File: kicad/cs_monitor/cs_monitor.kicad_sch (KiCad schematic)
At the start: 130 parts, among them J1 Conn_01x01_Female, J2 Conn_01x01_Female, J3 Conn_01x01_Female, J4 Conn, J5 Conn_01x01_Female, J6 Conn_01x01_Female, J7 Conn_01x01_Female, J8 Conn_01x01_Female, J9 Conn_01x01_Female, Q1 5N10, Q2 Q_NMOS_GSD, T1 HY931147C, U1 W5500, U2 OPA354AIDBVR, U3 LM2733XMF, U4 LMR50410XDBVR, U5 NCP1117-3.3, U6 MCP1700x, Y1 25MHz, Y2 16

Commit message: удалено:       kicad/cs_monitor/#auto_saved_files# 	удалено:       kicad/cs_monitor/_autosave-cs_monitor.kicad_pcb 	удалено:       kicad/cs_monitor/_autosave-cs_monitor.kicad_sch 	удалено:       kicad/cs_monitor/cs_monitor-backups/cs_monitor-2025-07-08_182651.zip 	удалено:       kicad/cs_monitor/cs_monitor-backups/cs_monitor-2025-07-08_184111.zip 	удалено:       kicad/cs_monitor/cs_monitor-backups/cs_monitor-2025-07-18_140158.zip 	удалено:       kicad/cs_monitor/cs_monitor-backups/cs_monitor-2025-07-18_141545.zip 	изменено:      kicad/cs_monitor/cs_monitor.kicad_pcb 	изменено:      kicad/cs_monitor/cs_monitor.kicad_prl 	изменено:      kicad/cs_monitor/cs_monitor.kicad_sch 	удалено:       kicad/cs_monitor/~_autosave-cs_monitor.kicad_pcb.lck 	удалено:       kicad/cs_monitor/~cs_monitor.kicad_sch.lck 	изменено:      stm32cubeide/SC_Monitor/Core/Inc/networkint.h 	изменено:      stm32cubeide/SC_Monitor/Core/Src/network_int.c 	изменено:      stm32cubeide/SC_Monitor/Release/Core/Src/AD5245.d 	изменено:      stm32cubeide/SC_Monitor/Release/Core/Src/main.d 	изменено:      stm32cubeide/SC_Monitor/Release/Core/Src/network_int.cyclo 	изменено:      stm32cubeide/SC_Monitor/Release/Core/Src/network_int.d 	изменено:      stm32cubeide/SC_Monitor/Release/Core/Src/network_int.o 	изменено:      stm32cubeide/SC_Monitor/Release/Core/Src/network_int.su 	изменено:      stm32cubeide/SC_Monitor/Release/Core/Src/ssd1306.d 	изменено:      stm32cubeide/SC_Monitor/Release/Core/Src/stm32g4xx_hal_msp.d 	изменено:      stm32cubeide/SC_Monitor/Release/Core/Src/stm32g4xx_it.d 	изменено:      stm32cubeide/SC_Monitor/Release/Core/Src/subdir.mk 	изменено:      stm32cubeide/SC_Monitor/Release/SC_Monitor.elf 	изменено:      stm32cubeide/SC_Monitor/Release/SC_Monitor.list 	изменено:      stm32cubeide/SC_Monitor/Release/SC_Monitor.map 	изменено:      stm32cubeide/SC_Monitor/Release/objects.list 	изменено:      stm32cubeide/WEB_Interface/test_line.html  	stm32cubeide/SC_Monitor/Core/Inc/webpages.h  	stm32cu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
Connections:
- net INT_ETH: now also D2.25 (pb11); no longer D2.26 (pb12)
- net SS_ETH: now also D2.26 (pb12); no longer D2.25 (pb11)
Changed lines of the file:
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@@
 	(global_label "INT_ETH"
 		(shape input)
-		(at 100.33 77.47 0)
+		(at 100.33 74.93 0)
 		(fields_autoplaced yes)
 		(effects
@@
 		)
 		(property "Intersheetrefs" "${INTERSHEET_REFS}"
-			(at 110.6328 77.47 0)
+			(at 110.6328 74.93 0)
 			(effects
 				(font
@@
 	(global_label "SS_ETH"
 		(shape input)
-		(at 100.33 74.93 0)
+		(at 100.33 77.47 0)
 		(fields_autoplaced yes)
 		(effects
@@
 		)
 		(property "Intersheetrefs" "${INTERSHEET_REFS}"
-			(at 110.1489 74.93 0)
+			(at 110.1489 77.47 0)
 			(effects
 				(font

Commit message: удалено:       kicad/cs_monitor/cs_monitor-backups/cs_monitor-2025-07-08_184829.zip 	удалено:       kicad/cs_monitor/cs_monitor-backups/cs_monitor-2025-07-08_185838.zip 	изменено:      kicad/cs_monitor/cs_monitor.kicad_pcb 	изменено:      kicad/cs_monitor/cs_monitor.kicad_pro 	изменено:      kicad/cs_monitor/cs_monitor.kicad_sch 	изменено:      kicad/cs_monitor/gerber/cs_monitor.drl 	удалено:       kicad/cs_monitor/gerber/cs_monitor_T01_0.30mm.gcode 	удалено:       kicad/cs_monitor/gerber/cs_monitor_T02_0.40mm.gcode 	удалено:       kicad/cs_monitor/gerber/cs_monitor_T03_0.70mm.gcode 	удалено:       kicad/cs_monitor/gerber/cs_monitor_T04_0.76mm.gcode 	удалено:       kicad/cs_monitor/gerber/cs_monitor_T05_1.00mm.gcode 	удалено:       kicad/cs_monitor/gerber/cs_monitor_T06_1.63mm.gcode 	изменено:      stm32cubeide/SC_Monitor/.mxproject 	изменено:      stm32cubeide/SC_Monitor/.settings/language.settings.xml 	изменено:      stm32cubeide/SC_Monitor/Core/Inc/main.h 	изменено:      stm32cubeide/SC_Monitor/Core/Src/main.c 	изменено:      stm32cubeide/SC_Monitor/Release/Core/Src/main.cyclo 	изменено:      stm32cubeide/SC_Monitor/Release/Core/Src/main.o 	изменено:      stm32cubeide/SC_Monitor/Release/Core/Src/main.su 	изменено:      stm32cubeide/SC_Monitor/Release/SC_Monitor.elf 	изменено:      stm32cubeide/SC_Monitor/Release/SC_Monitor.list 	изменено:      stm32cubeide/SC_Monitor/Release/SC_Monitor.map 	изменено:      stm32cubeide/SC_Monitor/SC_Monitor Release.launch 	изменено:      stm32cubeide/SC_Monitor/SC_Monitor.ioc
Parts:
- added C52: 10u, Capacitor_SMD:C_0402_1005Metric, symbol Device:C
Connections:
- net +3V3: now also C52.2
- net GND: now also C52.1
- net INT_ETH: now also D2.26 (pb12); no longer D2.25 (pb11)
- net SS_ETH: now also D2.25 (pb11); no longer D2.26 (pb12)
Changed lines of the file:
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@@
 	)
 	(junction
+		(at 101.6 22.86)
+		(diameter 0)
+		(color 0 0 0 0)
+	)
+	(junction
 		(at 80.01 114.3)
 		(diameter 0)
@@
 	(wire
 		(pts
+			(xy 101.6 22.86) (xy 106.68 22.86)
+		)
+		(stroke
+			(width 0)
+			(type default)
+		)
+	)
+	(wire
+		(pts
 			(xy 74.93 114.3) (xy 80.01 114.3)
 		)
@@
 	(wire
 		(pts
+			(xy 101.6 30.48) (xy 106.68 30.48)
+		)
+		(stroke
+			(width 0)
+			(type default)
+		)
+	)
+	(wire
+		(pts
 			(xy 41.91 137.16) (xy 43.18 137.16)
 		)
@@
 	(global_label "INT_ETH"
 		(shape input)
-		(at 100.33 74.93 0)
+		(at 100.33 77.47 0)
 		(fields_autoplaced yes)
 		(effects
@@
 		)
 		(property "Intersheetrefs" "${INTERSHEET_REFS}"
-			(at 110.6328 74.93 0)
+			(at 110.6328 77.47 0)
 			(effects
 				(font
@@
 	(global_label "SS_ETH"
 		(shape input)
-		(at 100.33 77.47 0)
+		(at 100.33 74.93 0)
 		(fields_autoplaced yes)
 		(effects
@@
 		)
 		(property "Intersheetrefs" "${INTERSHEET_REFS}"
-			(at 110.1489 77.47 0)
+			(at 110.1489 74.93 0)
 			(effects
 				(font
@@
 					(unit 1)
 				)
+			)
+		)
+	)
+	(symbol
+		(lib_id "Device:C")
+		(at 106.68 26.67 180)
+		(unit 1)
+		(exclude_from_sim no)
+		(in_bom yes)
+		(on_board yes)
+		(dnp no)
+		(property "Reference" "C52"
+			(at 106.68 19.685 0)
+			(effects
+				(font
+					(size 1.27 1.27)
+				)
+			)
+		)
+		(property "Value" "10u"
+			(at 106.68 21.59 0)
+			(effects
+				(font
+					(size 1.27 1.27)
+				)
+			)
+		)
+		(property "Footprint" "Capacitor_SMD:C_0402_1005Metric"
+			(at 105.7148 22.86 0)
+			(effects
+				(font
+					(size 1.27 1.27)
+				)
+				(hide yes)
+			)
+		)
+		(property "Datasheet" "~"
+			(at 106.68 26.67 0)
+			(effects
+				(font
+					(size 1.27 1.27)
+				)
+				(hide yes)
+			)
+		)
+		(property "Description" ""
+			(at 106.68 26.67 0)
+			(effects
+				(font
+					(size 1.27 1.27)
+				)
+			)
+		)
+		(pin "1"
+		)
+		(pin "2"
+		)
+		(instances
+			(project "cs_monitor"
+				(path "/b09d7ffb-630f-4d95-a1b6-b233a9d12a7e"
+					(reference "C52")
+					(unit 1)
+				)

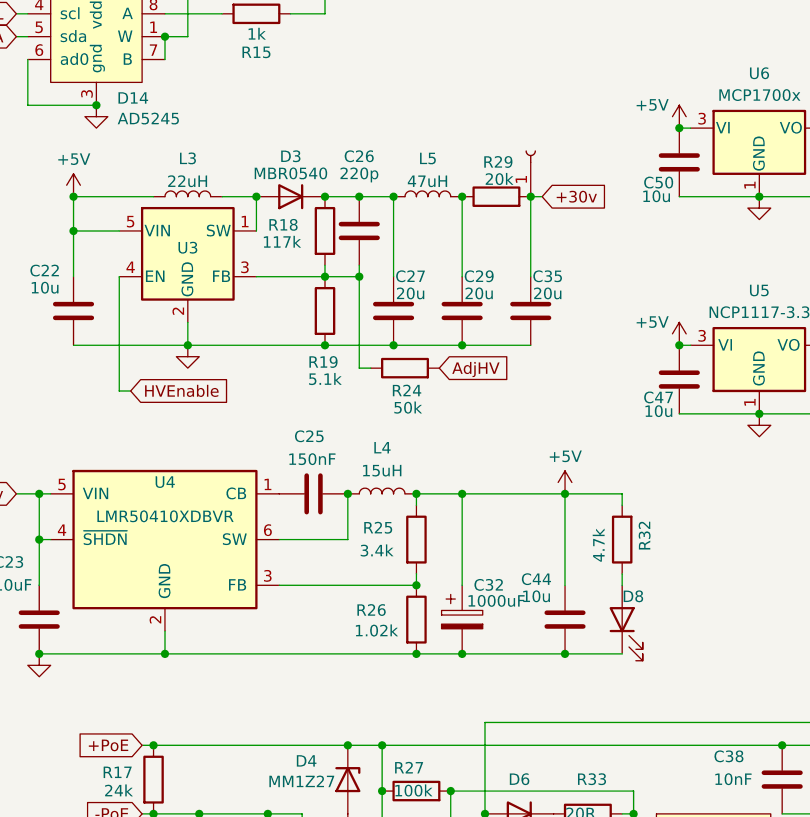
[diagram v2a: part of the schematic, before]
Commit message: новый файл:    kicad/cs_monitor/bom/ibom.html 	изменено:      kicad/cs_monitor/cs_monitor.kicad_pcb 	изменено:      kicad/cs_monitor/cs_monitor.kicad_sch 	изменено:      stm32cubeide/SC_Monitor/.mxproject 	изменено:      stm32cubeide/SC_Monitor/.settings/language.settings.xml 	изменено:      stm32cubeide/SC_Monitor/Core/Src/main.c 	изменено:      stm32cubeide/SC_Monitor/Release/Core/Src/main.cyclo 	изменено:      stm32cubeide/SC_Monitor/Release/Core/Src/main.o 	изменено:      stm32cubeide/SC_Monitor/Release/Core/Src/main.su 	изменено:      stm32cubeide/SC_Monitor/Release/SC_Monitor.elf 	изменено:      stm32cubeide/SC_Monitor/Release/SC_Monitor.list 	изменено:      stm32cubeide/SC_Monitor/Release/SC_Monitor.map 	изменено:      stm32cubeide/SC_Monitor/SC_Monitor.ioc
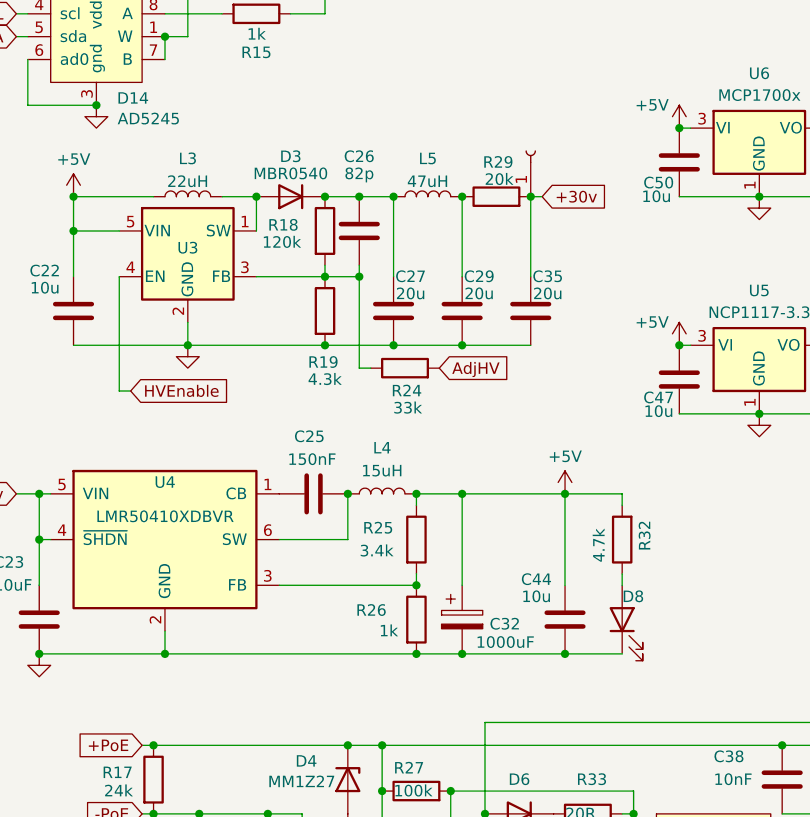
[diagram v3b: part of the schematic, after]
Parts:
- C26: value 220p -> 82p
- R18: value 117k -> 120k
- R19: value 5.1k -> 4.3k
- R24: value 50k -> 33k
- R26: value 1.02k -> 1k
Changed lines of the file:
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@@
 			)
 		)
-		(property "Value" "117k"
+		(property "Value" "120k"
 			(at 172.085 78.74 0)
 			(effects
@@
 			)
 		)
-		(property "Value" "1.02k"
+		(property "Value" "1k"
 			(at 187.198 121.92 0)
 			(effects
@@
 			)
 		)
-		(property "Value" "50k"
+		(property "Value" "33k"
 			(at 189.865 97.155 90)
 			(effects
@@
 			)
 		)
-		(property "Value" "5.1k"
+		(property "Value" "4.3k"
 			(at 177.165 93.98 0)
 			(effects
@@
 			)
 		)
-		(property "Value" "220p"
+		(property "Value" "82p"
 			(at 182.88 71.12 0)
 			(effects
@@
 		(dnp no)
 		(property "Reference" "C32"
-			(at 195.58 116.84 0)
+			(at 197.358 121.158 0)
 			(effects
 				(font
@@
 		)
 		(property "Value" "1000uF"
-			(at 194.818 118.618 0)
+			(at 195.834 123.19 0)
 			(effects
 				(font

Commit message: изменено:      kicad/cs_monitor/cs_monitor.kicad_sch
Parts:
- R18: value 120k -> 330k
- R19: value 4.3k -> 13k
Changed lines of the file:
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@@
 			)
 		)
-		(property "Value" "120k"
+		(property "Value" "330k"
 			(at 172.085 78.74 0)
 			(effects
@@
 			)
 		)
-		(property "Value" "4.3k"
+		(property "Value" "13k"
 			(at 177.165 93.98 0)
 			(effects

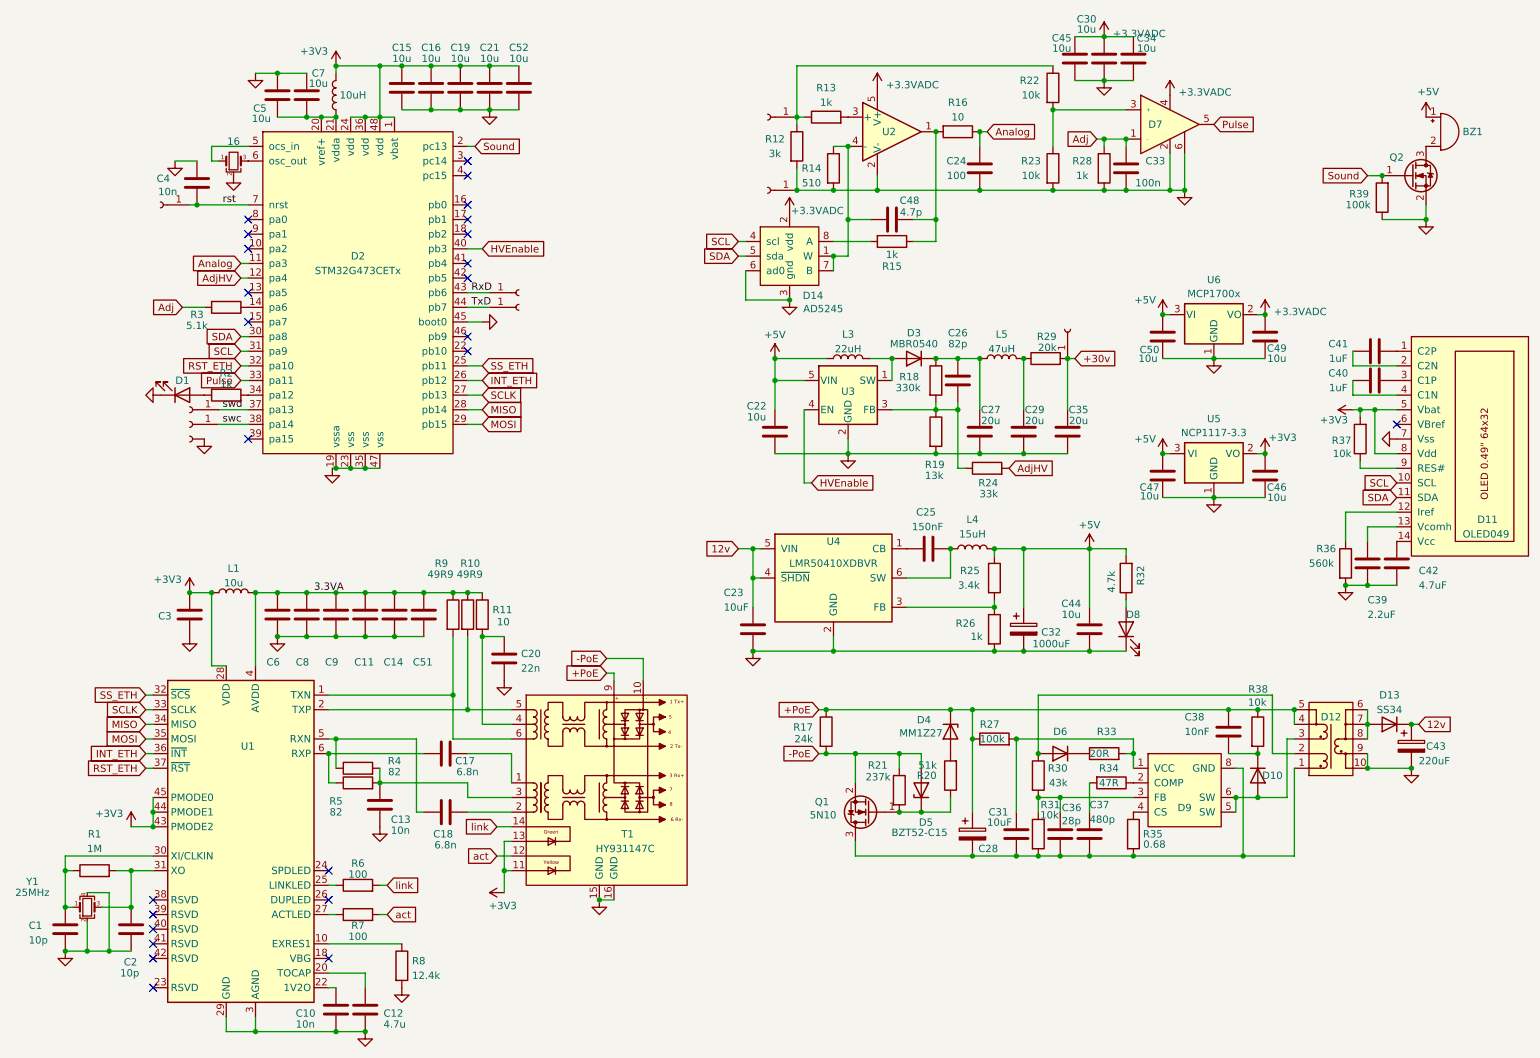
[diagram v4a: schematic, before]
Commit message: удалено:       kicad/cs_monitor/cs_monitor-backups/cs_monitor-2025-07-09_183647.zip 	удалено:       kicad/cs_monitor/cs_monitor-backups/cs_monitor-2025-07-09_190248.zip 	изменено:      kicad/cs_monitor/cs_monitor.kicad_pcb 	изменено:      kicad/cs_monitor/cs_monitor.kicad_sch
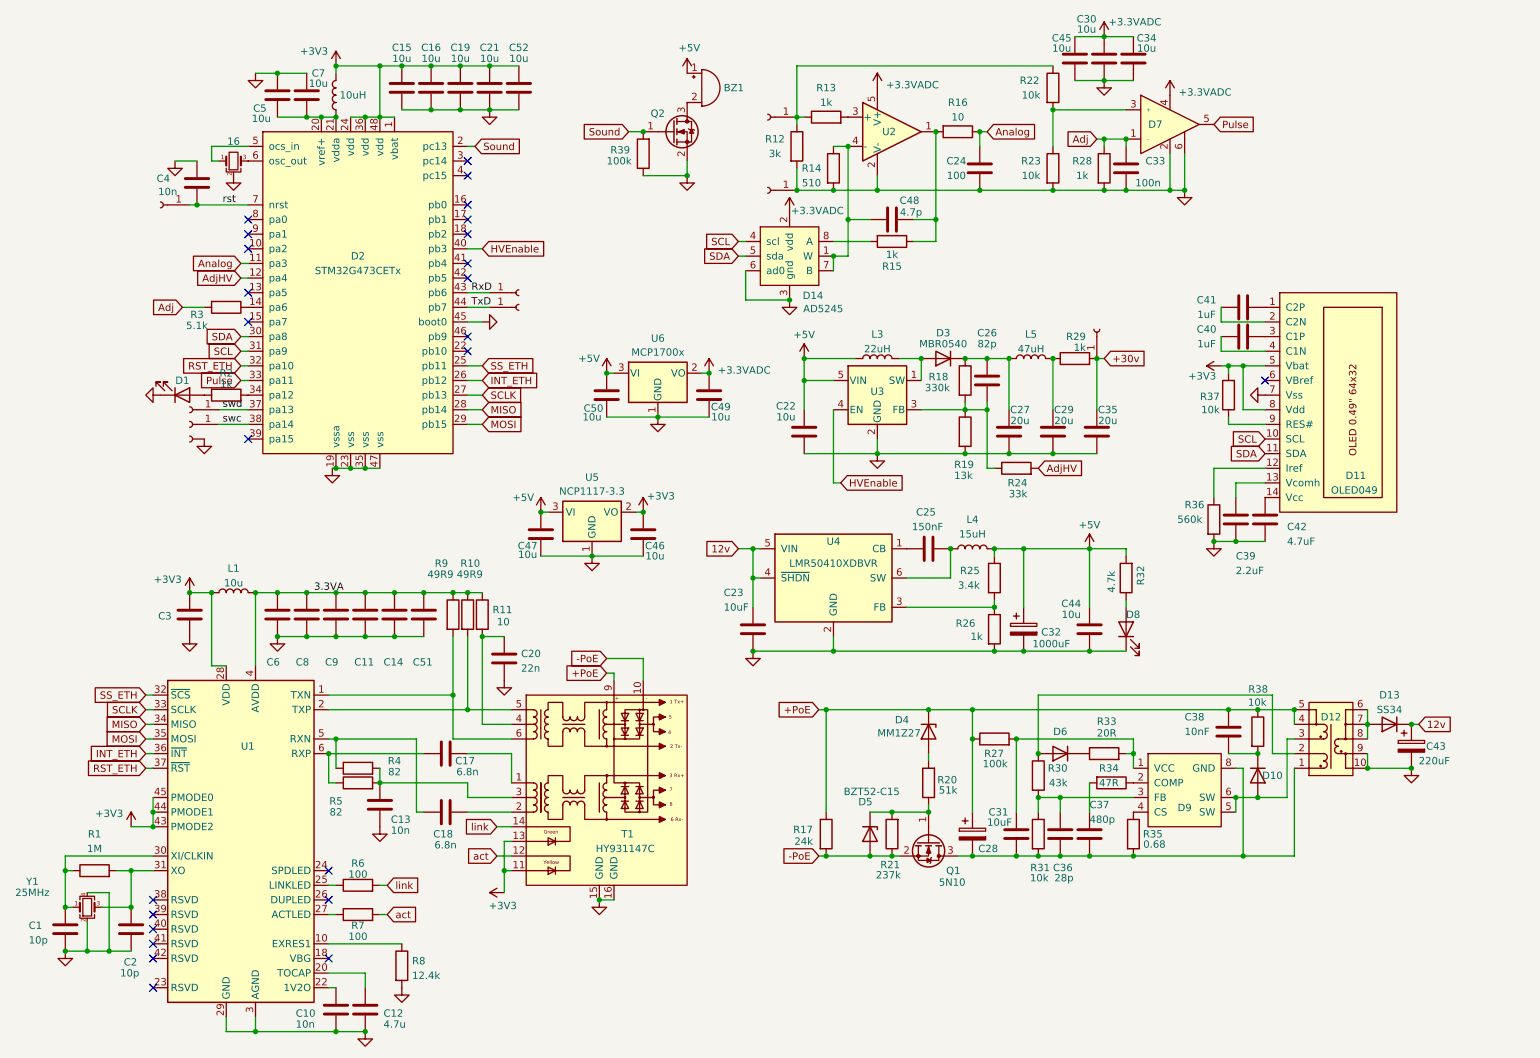
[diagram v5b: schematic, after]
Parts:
- R29: value 20k -> 1k
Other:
- moved on the sheet: BZ1, C22, C26, C27, C29, C35, C39, C40, C41, C42, C46, C47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

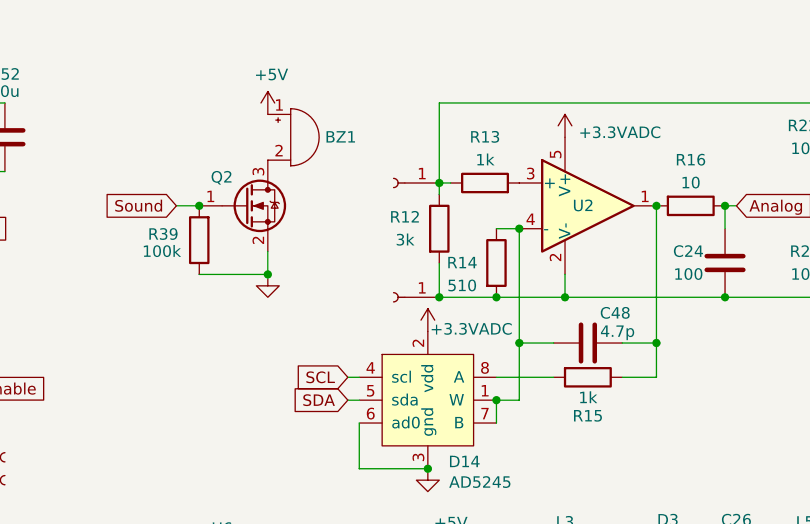
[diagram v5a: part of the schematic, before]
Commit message: изменено:      kicad/cs_monitor/cs_monitor.kicad_pcb 	изменено:      kicad/cs_monitor/cs_monitor.kicad_sch 	изменено:      stm32cubeide/SC_Monitor/Core/Inc/main.h 	изменено:      stm32cubeide/SC_Monitor/Core/Src/main.c 	изменено:      stm32cubeide/SC_Monitor/Release/Core/Src/main.o 	изменено:      stm32cubeide/SC_Monitor/Release/SC_Monitor.elf 	изменено:      stm32cubeide/SC_Monitor/Release/SC_Monitor.list 	изменено:      stm32cubeide/SC_Monitor/Release/SC_Monitor.map 	изменено:      stm32cubeide/SC_Monitor/SC_Monitor.ioc
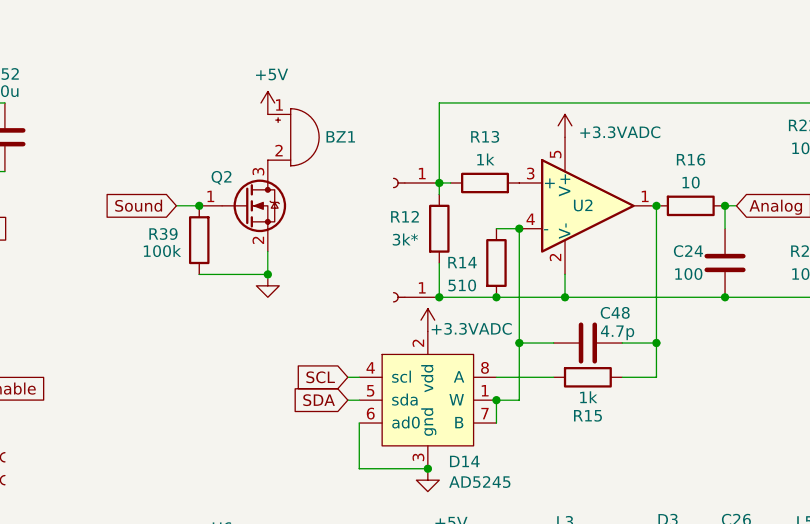
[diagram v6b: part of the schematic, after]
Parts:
- R12: value 3k -> 3k*
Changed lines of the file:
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@@
 			)
 		)
-		(property "Value" "3k"
+		(property "Value" "3k*"
 			(at 151.13 38.1 0)
 			(effects
